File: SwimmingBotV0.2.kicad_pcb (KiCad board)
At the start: 2 copper layers, 70 x 51 mm, 137 parts, among them P10 ANT, P11 DEBUG, P2 ANALOG, P3 CHRG, P4 BATT, P5 DEBUG_JUMPER, P6 FIN1, P7 FIN2, P8 MOT1, P9 MOT2, Q1 Q_NMOS_DGS, Q10 PMV45EN2, Q11 PMV45EN2, Q12 PMV45EN2, Q13 PMV45EN2, Q14 PMV45EN2, Q15 PMV45EN2, Q2 Q_PMOS_DGS, Q3 Q_NMOS_DGS, Q4 PMV45EN2, Q5 PMV45EN2, Q6 PMV45EN2, Q7 PMV45EN2, Q8 PMV45EN2, Q9 PMV45EN2, U1 LT3470A, U10 TPS6216X, U2 MCP73834, U3 A4960, U4 A4960, U5 HUM-900-PRO, U6 MPU-9250, U8 MAX6034_25, U9 STM32F446-144, X1 CRYSTAL_SMD, Y1 Crystal

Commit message: sketched board outline layer, it is currently conservative.  Also removed obvious offenders from previous layout
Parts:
- removed C49, C50, C8, C9: 100nF, Capacitors_SMD:C_0402
- removed D4, D5: LED, LEDs:LED_0603
- removed JP1: JUMPER, Custom_Footprints:JUMPER
- removed MEM1: IS42S16160G, Custom_Footprints:TSOP-54
- removed MEM2: S29GL256S, Custom_Footprints:TSOP-56_TYPE_1
- removed R15: 10K, Resistors_SMD:R_0402
- removed R17, R20: 1k, Resistors_SMD:R_0402
- removed U9: STM32F446-144, Housings_QFP:LQFP-144_20x20mm_Pitch0.5mm
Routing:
- net (no net): track 0.00 -> 1297.5 mm, vias 0 -> 92
- net /Digital/DQ5: track 93.1 -> 0.00 mm, vias 3 -> 0
- net /Digital/DQ4: track 92.0 -> 0.00 mm, vias 1 -> 0
- net /Digital/DQ6: track 91.0 -> 0.00 mm, vias 3 -> 0
- net /Digital/DQ0: track 89.1 -> 0.00 mm, vias 3 -> 0
- net /Digital/DQ1: track 88.6 -> 0.00 mm, vias 3 -> 0
- net /Digital/DQ2: track 82.1 -> 0.00 mm, vias 3 -> 0
- net GND: track 642.9 -> 561.3 mm, vias 90 -> 83
- net /Digital/A15: track 81.6 -> 0.00 mm, vias 3 -> 0
- net /Digital/A14: track 81.3 -> 0.00 mm, vias 3 -> 0
- net /Digital/DQ3: track 76.6 -> 0.00 mm, vias 1 -> 0
- net /Digital/3.3V: track 310.0 -> 240.7 mm, vias 29 -> 23
- net /Digital/A12: track 65.3 -> 0.00 mm, vias 1 -> 0
- net /Digital/A5: track 61.3 -> 0.00 mm, vias 3 -> 0
- net /Digital/A4: track 60.4 -> 0.00 mm, vias 3 -> 0
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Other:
- board size 70 x 51 mm -> 146.8 x 152 mm

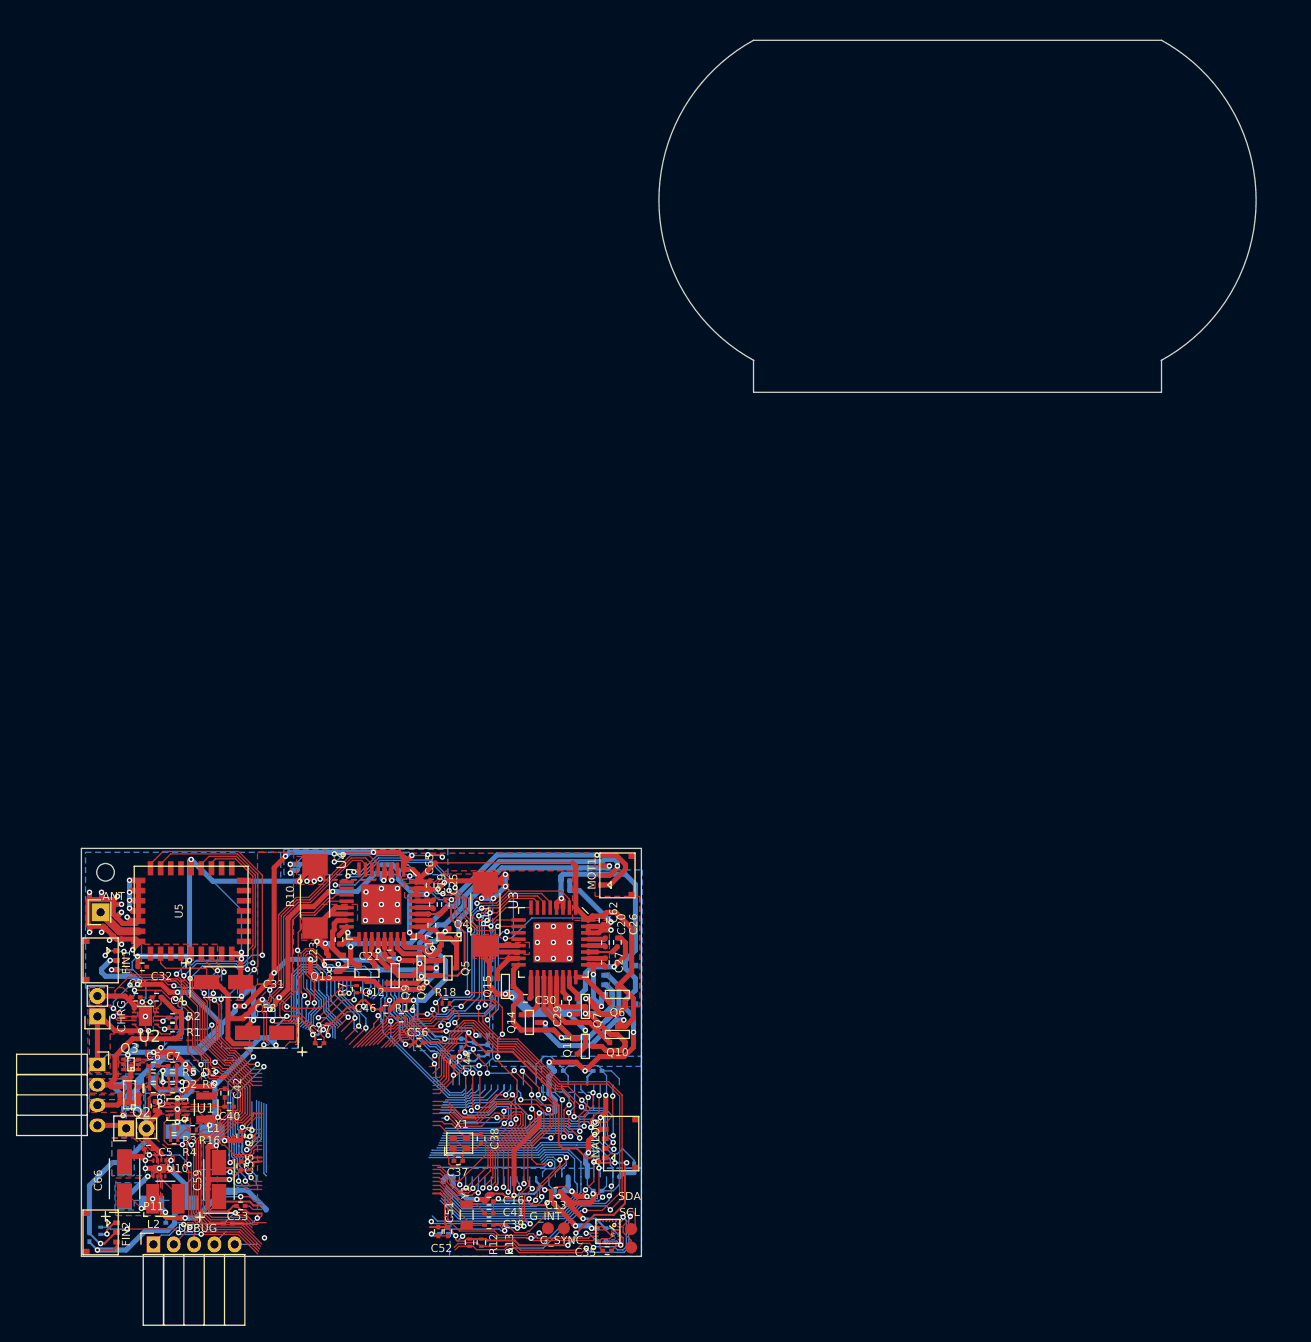
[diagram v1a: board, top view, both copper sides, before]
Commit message: pcb started in earnest, footprint changes in schematics, about to rename v0.2 boardfile to v0.1, kicad needs the same filename to have backrefs for net highlighting
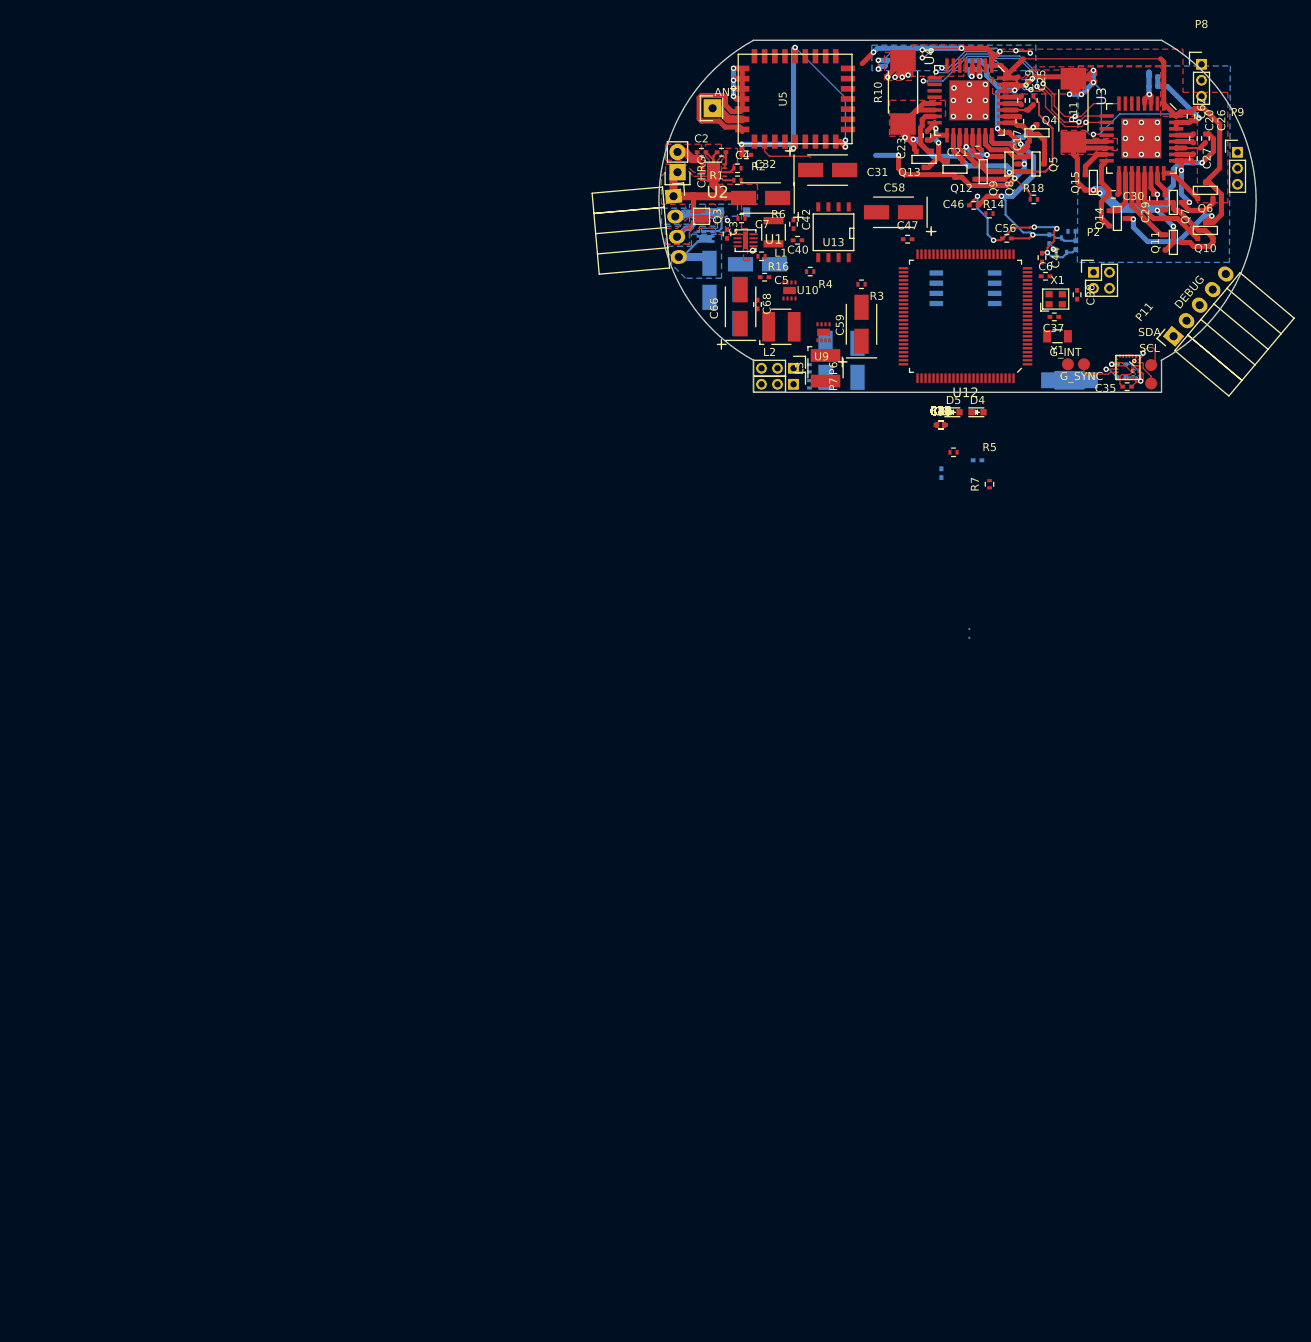
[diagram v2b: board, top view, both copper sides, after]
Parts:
- removed C13, C14, C15, C16, C52, C53, C54, C55, C57: 100nF, Capacitors_SMD:C_0402
- removed C64, C65: 1uF, Capacitors_SMD:C_0402
- removed D2, D3: D_Schottky, Custom_Footprints:D_0402_SOD_923
- removed P5: DEBUG_JUMPER, Socket_Strips:Socket_Strip_Straight_1x02
- removed REF**: MountingHole_2.2mm_M2, Mounting_Holes:MountingHole_2.2mm_M2
- added C36, C48, C49, C50, C8, C9: 100nF, Capacitors_SMD:C_0402, F.Cu at (119.4, 94.1)
- added D4: LED, LEDs:LED_0603, F.Cu at (124.0, 92.5)
- added D5: LED, LEDs:LED_0603, F.Cu at (121.0, 92.5)
- added JP1: JUMPER, Oddities:NetTie-I_Connected_SMD, B.Cu at (135.5, 88.5)
- added L3: 2.2uH, Inductors:NR4018, F.Cu at (105.0, 87.0)
- added R15: 10K, Resistors_SMD:R_0402, F.Cu at (119.4, 94.1)
- added R17, R20: 1k, Resistors_SMD:R_0402, F.Cu at (119.4, 94.1)
- added R21, R22, R23: 10k, Resistors_SMD:R_0402, F.Cu at (119.4, 94.1)
- added U11: SST26VF064B, Housings_SOIC:SOIJ-8_5.3x5.3mm_Pitch1.27mm, B.Cu at (122.5, 77.0)
- added U12: STM32F446-100, Custom_Footprints:STM32F446_QFP_100, F.Cu at (122.5, 80.5)
- added U13: LTC1163, SMD_Packages:SOIC-8-N, F.Cu at (106.0, 70.0)
- added U9: TPS6216X, Custom_Footprints:WSON-8, F.Cu at (104.5, 82.5)
- C10, C11: value 100nF -> 10uF; footprint Capacitors_SMD:C_0402 -> Capacitors_Tantalum_SMD:TantalC_SizeB_EIA-3528_HandSoldering
- C12: value 100nF -> 1uF; moved to F.Cu
- C6: value 1nF -> 1uF
- C68: moved to F.Cu
- C7: value 1nF -> 10uF; footprint Capacitors_SMD:C_0402 -> Capacitors_Tantalum_SMD:TantalC_SizeB_EIA-3528_HandSoldering
- P2: footprint Custom_Footprints:PICO-EZMATE-4 -> Pin_Headers:Pin_Header_Straight_2x02_Pitch2.00mm
- P6, P7, P8: footprint Custom_Footprints:PICO-EZMATE-3 -> Pin_Headers:Pin_Header_Straight_1x03_Pitch2.00mm
- P9: footprint Custom_Footprints:PICO-EZMATE-3 -> Pin_Headers:Pin_Header_Straight_1x03_Pitch2.00mm; moved to F.Cu
- Q1, Q3: footprint Custom_Footprints:SC-70-6-DGS -> Custom_Footprints:SC-70-ENHANCED-DGS
- Q2: value Q_PMOS_DGS -> Q_NMOS_DGS; footprint Custom_Footprints:TSOP-6_Si3407DV -> Custom_Footprints:SC-70-ENHANCED-DGS; moved to B.Cu
- R1: value 10k -> 5k
- R19: value 10k -> 4.1k-3.9k
- R5: value 10k -> 65k
- moved P11 170.7 mm to (148.5, 83.0), turned to 50 degrees
- moved C6 148.9 mm to (132.5, 75.5)
- moved C63 143.0 mm to (119.5, 100.1)
- moved R9 138.0 mm to (103.0, 89.0)
- moved C68 136.3 mm to (96.5, 79.0), turned to 90 degrees
- moved R3 136.1 mm to (109.5, 76.5)
- moved P7 135.9 mm to (101.0, 89.0)
- moved U10 135.1 mm to (100.8, 77.3)
- moved R4 134.5 mm to (103.1, 74.9)
- moved C1 134.1 mm to (90.5, 76.0)
- moved C59 133.7 mm to (109.5, 81.5)
- moved C60 133.7 mm to (124.0, 98.5)
- moved C5 133.5 mm to (97.4, 75.6)
- moved C66 133.5 mm to (94.4, 79.3)
- moved L2 133.5 mm to (99.5, 81.8)
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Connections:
- C10 pad 1: GND -> /Motors/VFIN
- C10 pad 2: /Digital/3.3V -> GND
- C11 pad 1: GND -> /Motors/VFIN
- C11 pad 2: /Digital/3.3V -> GND
- C12 pad 2: /Digital/3.3V -> /Motors/VFIN
- C6 pad 1: Net-(C6-Pad1) -> /Micro/A0
- C7 pad 1: Net-(C7-Pad1) -> /Charge/2S
- P4 pad 4: /Charge/2S_RAW -> /Charge/2S
- P6 pad 2: /Charge/2S -> /Motors/VFIN
- P7 pad 2: /Charge/2S -> /Motors/VFIN
- Q1 pad 2: Net-(C7-Pad1) -> /Charge/GATE2
- Q2 pad 1: /Charge/2S_NEG -> /Charge/1S
- Q2 pad 2: Net-(C6-Pad1) -> /Charge/GATE3
- Q2 pad 3: /Charge/1S -> /Charge/2S_NEG
- Q3 pad 2: Net-(C7-Pad1) -> /Charge/GATE1
- R1 pad 2: GND -> Net-(R1-Pad2)
- R14 pad 1: /Micro/SDIO_CLK -> /Charge/5V_CHG
- R14 pad 2: GND -> Net-(R14-Pad2)
- R5 pad 1: /Charge/2S_EN -> /Motors/VFIN
- R5 pad 2: Net-(C6-Pad1) -> Net-(R5-Pad2)
- R6 pad 1: /Charge/2S_EN -> GND
- R6 pad 2: Net-(C7-Pad1) -> Net-(R5-Pad2)
- R7 pad 1: /Micro/FMC_NWAIT -> /Charge/1S
- R7 pad 2: /Digital/3.3V -> /Micro/PA8
- U1 pad 7: Net-(U1-Pad7) -> (no net)
- U1 pad 8: /Micro/PG12 -> /Micro/PA8
- U2 pad 6: /Charge/CHG_EN# -> Net-(R1-Pad2)
- U2 pad 7: /Charge/CHG_TE# -> Net-(R14-Pad2)
- U3 pad PAD: Net-(U3-PadPAD) -> (no net)
- U4 pad PAD: Net-(U4-PadPAD) -> (no net)
- U5 pad 1: Net-(U5-Pad1) -> (no net)
- U5 pad 10: Net-(U5-Pad10) -> (no net)
- U5 pad 11: Net-(U5-Pad11) -> (no net)
- U5 pad 12: /Micro/PG7 -> /Micro/PD15
- U5 pad 13: /Micro/PG6 -> /Micro/PE1
- U5 pad 2: Net-(U5-Pad2) -> (no net)
- U5 pad 23: Net-(U5-Pad23) -> (no net)
- U5 pad 24: Net-(U5-Pad24) -> (no net)
- U5 pad 28: Net-(U5-Pad28) -> /rf/RF_CTS
- U5 pad 3: Net-(U5-Pad3) -> (no net)
- U5 pad 30: Net-(U5-Pad30) -> (no net)
- U5 pad 31: Net-(U5-Pad31) -> /Micro/PE13
- U5 pad 32: Net-(U5-Pad32) -> (no net)
- U5 pad 4: Net-(U5-Pad4) -> (no net)
- U5 pad 5: Net-(U5-Pad5) -> (no net)
- U5 pad 6: Net-(U5-Pad6) -> (no net)
- U6 pad 14: Net-(U6-Pad14) -> (no net)
- U6 pad 15: Net-(U6-Pad15) -> (no net)
- U6 pad 16: Net-(U6-Pad16) -> (no net)
- U6 pad 17: Net-(U6-Pad17) -> (no net)
- U6 pad 19: Net-(U6-Pad19) -> (no net)
- U6 pad 2: Net-(U6-Pad2) -> (no net)
- U6 pad 21: /Sensors/AUX_SDA -> (no net)
- U6 pad 3: Net-(U6-Pad3) -> (no net)
- U6 pad 4: Net-(U6-Pad4) -> (no net)
- U6 pad 5: Net-(U6-Pad5) -> (no net)
- U6 pad 6: Net-(U6-Pad6) -> (no net)
- U6 pad 7: /Sensors/AUX_SCL -> (no net)
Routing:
- net (no net): track 1297.5 -> 4.10 mm, vias 92 -> 18
- net GND: track 561.3 -> 222.1 mm, vias 83 -> 27
- net /Digital/3.3V: track 240.7 -> 31.5 mm, vias 23 -> 4
- net /Power/CHG_CTL_VCC: track 211.0 -> 25.0 mm, vias 22 -> 5
- net /Charge/2S: track 280.5 -> 170.2 mm, vias 23 -> 16
- net /Micro/PG6: track 72.1 -> 0.00 mm, vias 2 -> 0
- net /Motors/MOT2_TACH: track 72.6 -> 0.67 mm, vias 4 -> 0
- net /Micro/PG7: track 61.5 -> 0.00 mm, vias 4 -> 0
- net /Motors/SDO: track 89.9 -> 28.9 mm, vias 5 -> 3
- net /Charge/5V_CHG: track 65.9 -> 5.09 mm
- net /Charge/CHG_STAT2: track 57.4 -> 0.00 mm, vias 4 -> 0
- net /Motors/FIN1: track 54.1 -> 0.00 mm, vias 1 -> 0
- net /Motors/MOT1_RESET#: track 52.1 -> 0.70 mm, vias 6 -> 0
- net /Micro/PB15: track 48.0 -> 0.53 mm, vias 2 -> 0
- net /Motors/C1: track 55.3 -> 9.65 mm, vias 3 -> 2
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- added copper zone on B.Cu, net /Charge/2S_NEG
- removed copper zone on F.Cu, net /Power/CHG_CTL_VCC
- removed copper zone on F.Cu, net Net-(C40-Pad1)
- removed copper zone on F.Cu, net Net-(L2-Pad2)
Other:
- board size 146.8 x 152 mm -> 74.7 x 44 mm
